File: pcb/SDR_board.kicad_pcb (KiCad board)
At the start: 4 copper layers, 100 x 100 mm, 469 parts, among them J1 USB_B_Mini, J201 Molex 73251-1150 SMA, J301 Molex 73251-1150 SMA, J401 Molex 73251-1150 SMA, J501 Molex 73251-1150 SMA, SW1 SW_Push, U1 AMS1117-3.3, U2 NB3L553, U201 BGA2803, U202 MSi001-Q40, U203 MAX19777AZA+, U204 ADS7883, U205 LMV712-N, U206 MAX19777AZA+, U207 ADS7883, U3 CY7C68013A-56PVX, U301 BGA2803, U302 MSi001-Q40, U303 MAX19777AZA+, U304 ADS7883, U305 LMV712-N, U306 MAX19777AZA+, U307 ADS7883, U401 BGA2803, U402 MSi001-Q40, U403 MAX19777AZA+, U404 ADS7883, U405 LMV712-N, U406 MAX19777AZA+, U407 ADS7883, U5 24LC128, U501 BGA2803, U502 MSi001-Q40, U503 MAX19777AZA+, U504 ADS7883, U505 LMV712-N, U506 MAX19777AZA+, U507 ADS7883, U6 MCP1825S, X1 XO32, X2 XO32

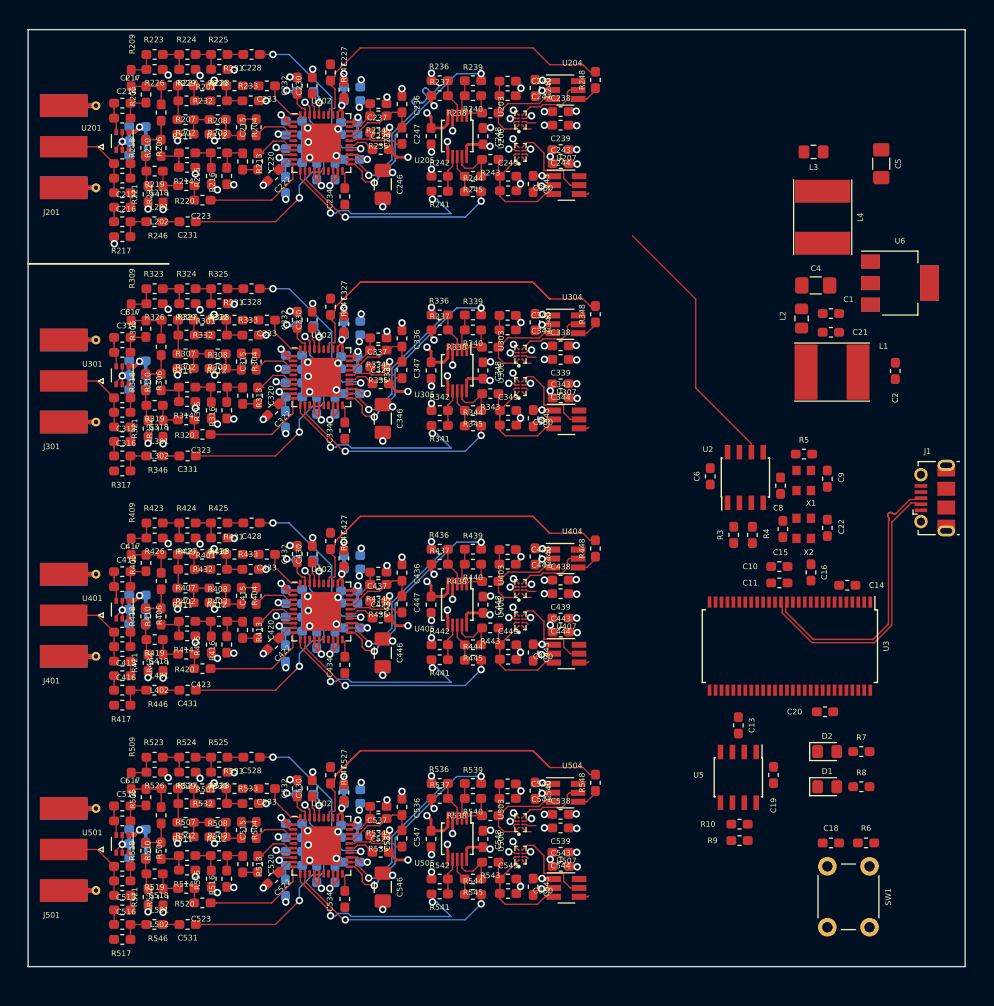
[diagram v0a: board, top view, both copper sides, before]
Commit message: silkscreen looks good for channel 1; TODO: copy to other channels.
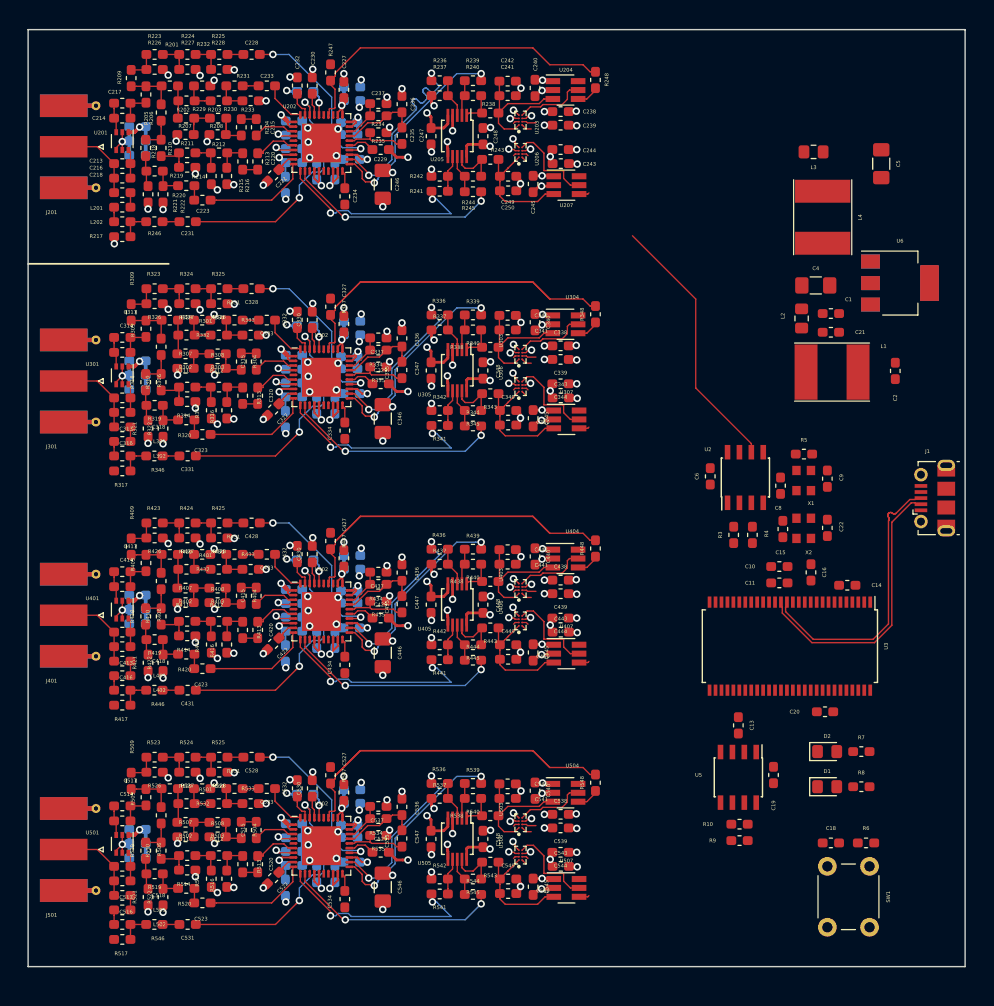
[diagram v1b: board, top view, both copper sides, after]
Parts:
- moved R202 0.16 mm to (41.9, 29.4)
- moved R203 0.16 mm to (45.3, 29.4)
- moved R207 0.05 mm to (41.8, 31.2)
- moved R208 0.05 mm to (45.2, 31.2)
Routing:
- net Net-(R203-Pad1): track 3.26 -> 5.03 mm
- net Net-(R202-Pad1): track 3.23 -> 4.02 mm
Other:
- rule pad_to_mask_clearance: 0.051 -> 0.03
- rule solder_mask_min_width: 0.25 -> 0.1

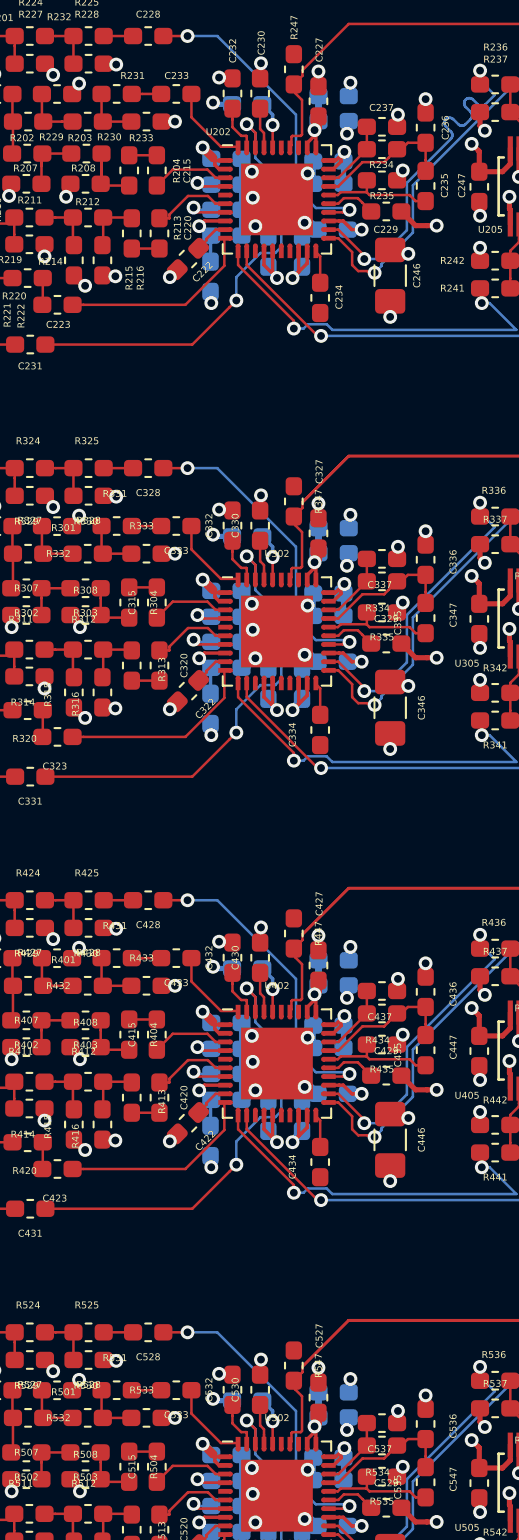
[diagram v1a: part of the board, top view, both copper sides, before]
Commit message: Closed solder resist around the MSi001 packages
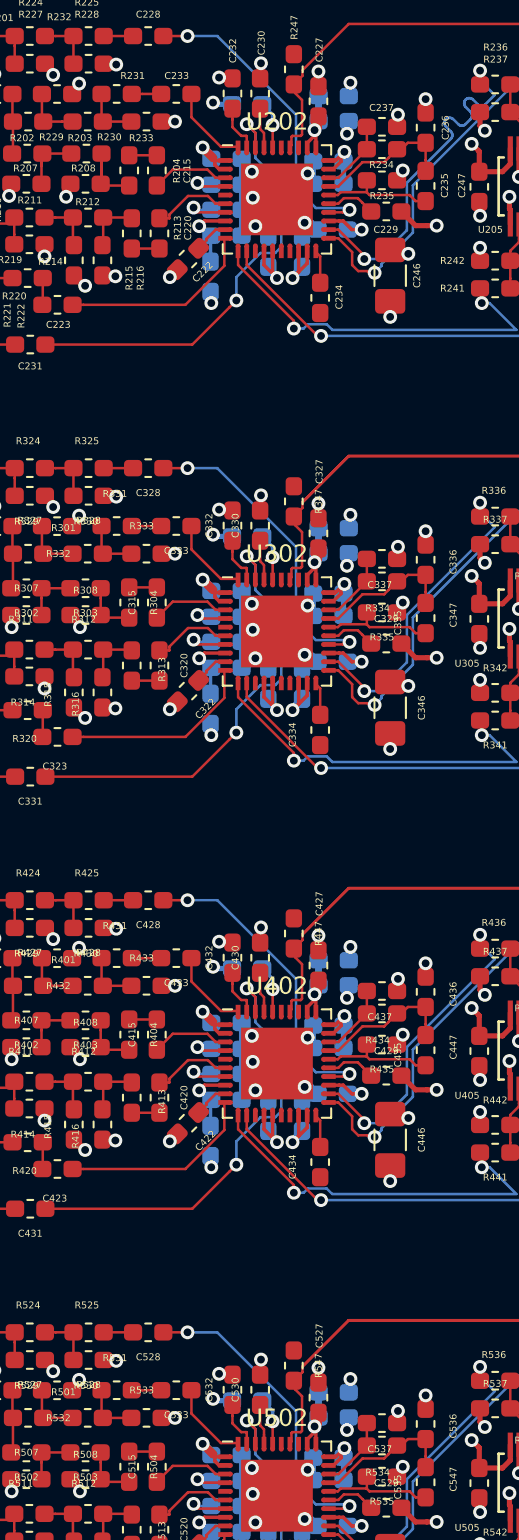
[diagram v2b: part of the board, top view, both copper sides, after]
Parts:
- U202, U302, U402, U502: footprint Package_DFN_QFN:Texas_S-PVQFN-N40_EP4.15x4.15mm -> footprints:Texas_S-PVQFN-N40_EP4.15x4.15mm_less_solder_resist

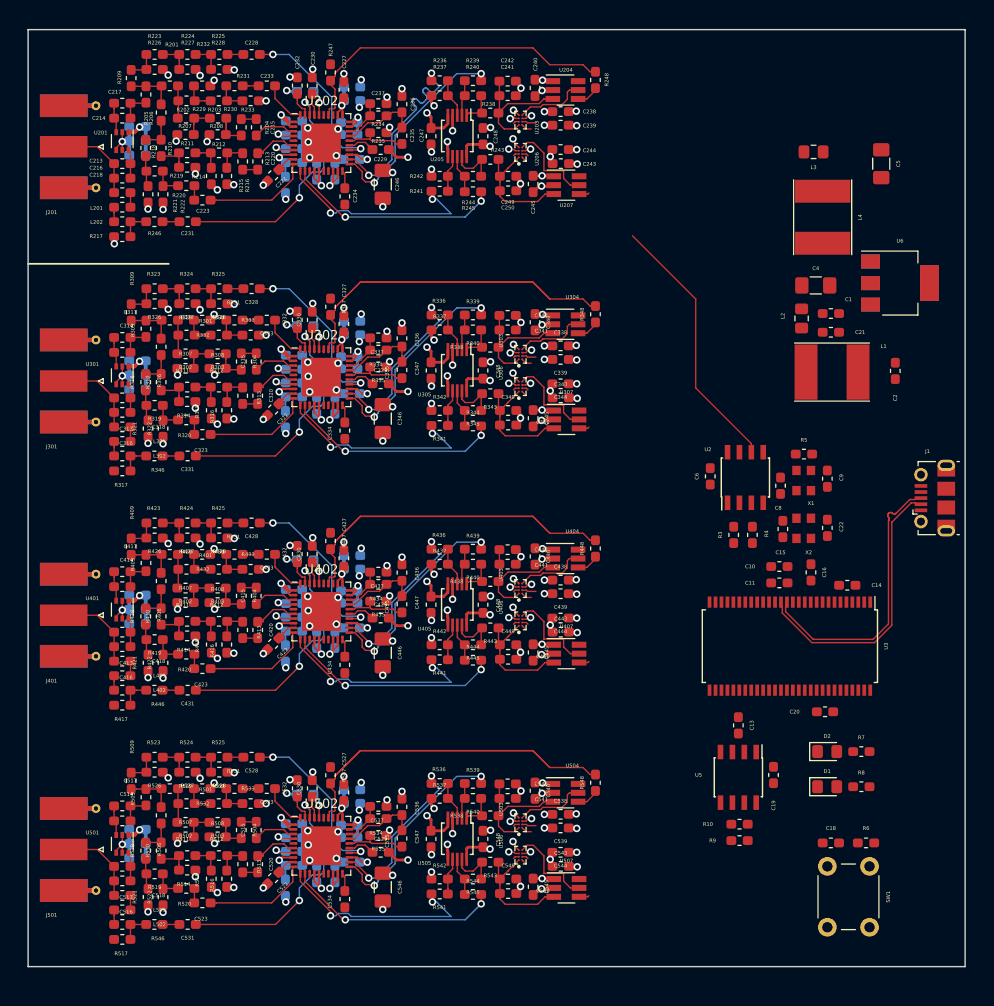
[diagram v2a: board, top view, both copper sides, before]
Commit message: Duplicated all those changes to chanel 1 through to the other channels
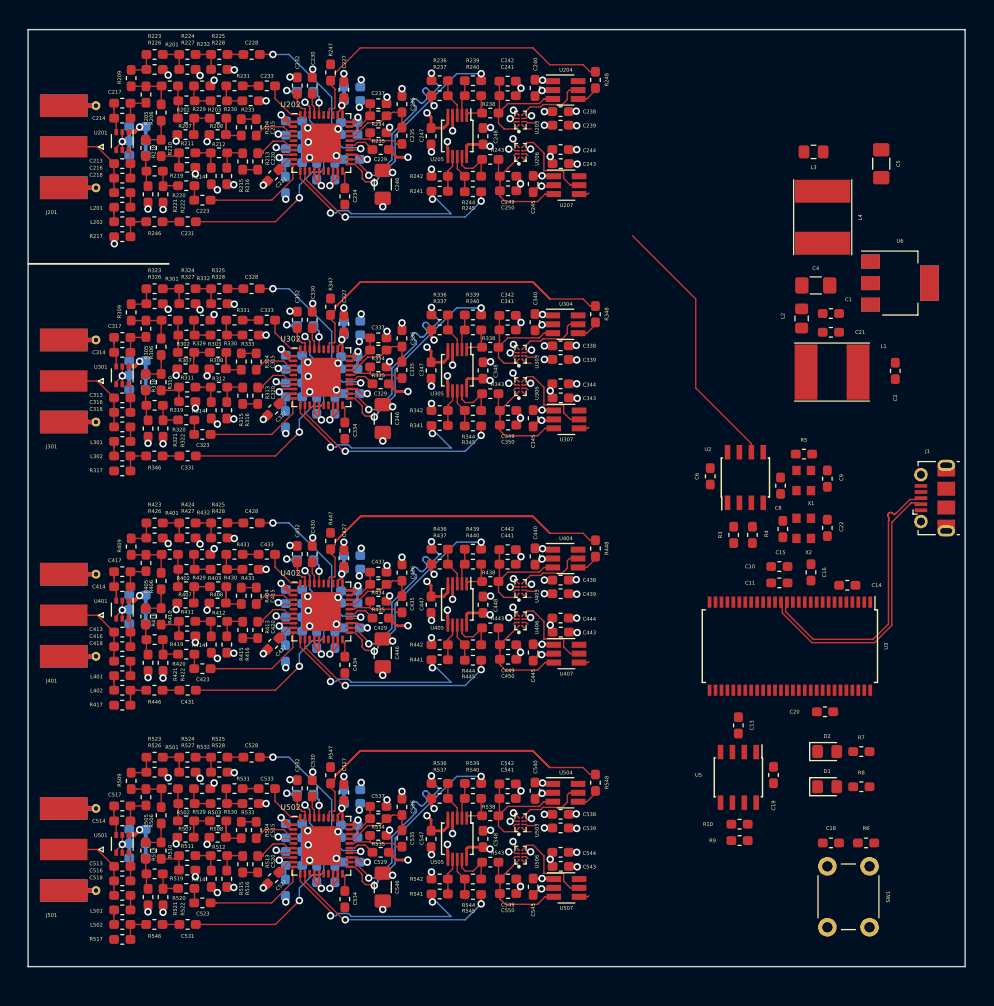
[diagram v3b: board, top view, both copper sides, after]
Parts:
- moved R302 0.16 mm to (41.9, 54.5)
- moved R303 0.16 mm to (45.3, 54.5)
- moved R402 0.16 mm to (41.9, 79.5)
- moved R502 0.16 mm to (41.9, 104.5)
- moved R403 0.16 mm to (45.3, 79.5)
- moved R503 0.16 mm to (45.3, 104.5)
- moved R307 0.05 mm to (41.8, 56.2)
- moved R308 0.05 mm to (45.2, 56.2)
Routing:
- net Net-(R347-Pad2): track 60.1 -> 109.6 mm
- net Net-(R547-Pad2): track 60.1 -> 109.6 mm
- net Net-(R447-Pad2): track 60.1 -> 109.6 mm
- net /Channel 2/Q_P: track 18.7 -> 21.7 mm
- net /Channel 4/Q_P: track 18.7 -> 21.7 mm
- net /Channel 3/Q_P: track 18.7 -> 21.7 mm
- net Net-(R303-Pad1): track 3.26 -> 5.03 mm
- net Net-(R503-Pad1): track 3.26 -> 5.03 mm
- net Net-(R403-Pad1): track 3.26 -> 5.03 mm
- net Net-(R302-Pad1): track 3.23 -> 4.02 mm
- net Net-(R502-Pad1): track 3.23 -> 4.02 mm
- net Net-(R402-Pad1): track 3.23 -> 4.02 mm
- net /Channel 4/Q_N: track 21.8 -> 22.6 mm
- net /Channel 3/Q_N: track 21.8 -> 22.6 mm
- net /Channel 2/Q_N: track 21.8 -> 22.6 mm

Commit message: simplified SPI clock source for the MSi001
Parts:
- removed R247, R248, R347, R348, R447, R448, R547, R548: 0R, Resistor_SMD:R_0603_1608Metric_Pad1.05x0.95mm_HandSolder
- added R1: 25, Resistor_SMD:R_0603_1608Metric_Pad1.05x0.95mm_HandSolder, F.Cu at (100.3, 61.6)
- added R2: 25, Resistor_SMD:R_0603_1608Metric_Pad1.05x0.95mm_HandSolder, F.Cu at (102.4, 61.6)
- moved C240 1.20 mm to (79.1, 25.0)
- moved U204 1.20 mm to (82.3, 25.2)
- moved C245 1.00 mm to (78.9, 37.5)
- moved U207 1.00 mm to (82.5, 37.6)
- moved C238 0.55 mm to (82.2, 28.4)
- moved C239 0.55 mm to (82.2, 29.8)
- moved C243 0.38 mm to (82.2, 34.4)
- moved C244 0.38 mm to (82.2, 32.9)
- moved C227 0.30 mm to (59.0, 26.4)
- moved R4 0.15 mm to (102.4, 73.9)
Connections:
- U2 pad 6: /TUNER_1_CLK -> Net-(R2-Pad1)
- U2 pad 7: /TUNER_2_CLK -> Net-(R1-Pad1)
- U202 pad 34: Net-(R247-Pad2) -> TUNER_SPI_CLK
- U302 pad 34: Net-(R347-Pad2) -> TUNER_SPI_CLK
- U402 pad 34: Net-(R447-Pad2) -> TUNER_SPI_CLK
- U502 pad 34: Net-(R547-Pad2) -> TUNER_SPI_CLK
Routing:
- net TUNER_SPI_CLK: track 0.00 -> 366.4 mm
- net Net-(R547-Pad2): track 109.6 -> 0.00 mm
- net Net-(R447-Pad2): track 109.6 -> 0.00 mm
- net Net-(R347-Pad2): track 109.6 -> 0.00 mm
- net TUNER_SPI_MOSI: track 0.00 -> 38.1 mm
- net /TUNER_1_nCS: track 0.00 -> 36.7 mm
- net Net-(R247-Pad2): track 35.3 -> 0.00 mm
- net /TUNER_1_CLK: track 28.4 -> 0.00 mm
- net ADC_nCS: track 8.90 -> 24.8 mm, vias 0 -> 2
- net ADC_CLK: track 23.7 -> 36.5 mm
- net /Channel 1/I_DOUT: track 9.73 -> 9.03 mm
- net +3.3VA: track 201.8 -> 201.6 mm, vias 76 -> 75

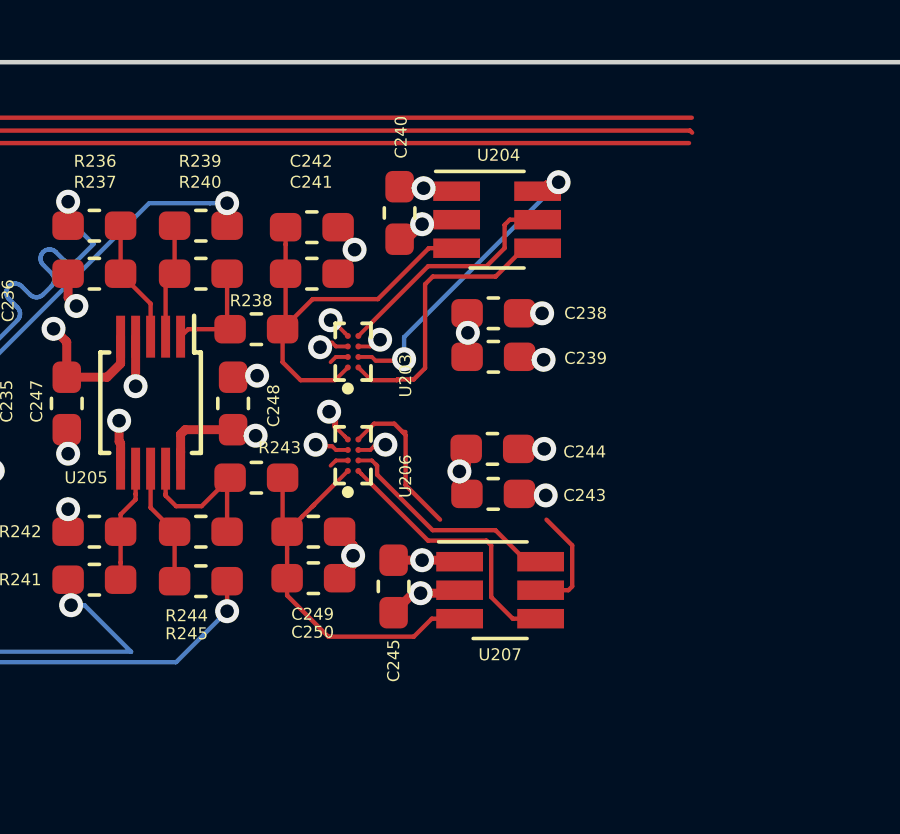
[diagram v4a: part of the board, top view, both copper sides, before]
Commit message: Finished signal routing for ADCs at the tuner side
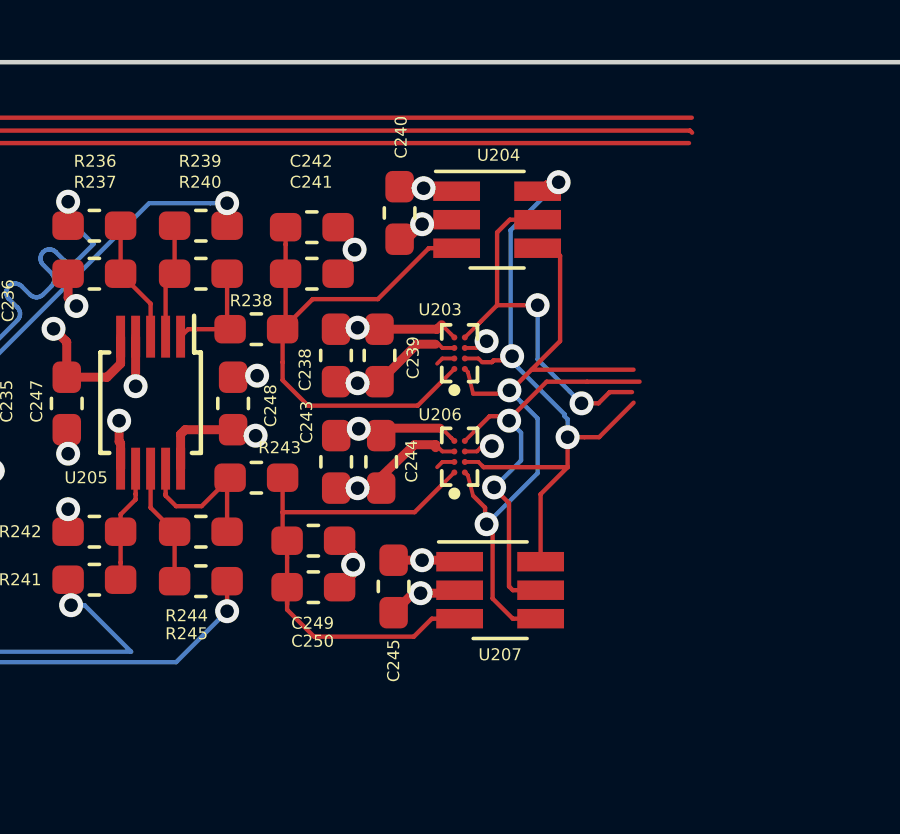
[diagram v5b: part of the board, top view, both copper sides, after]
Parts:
- moved C243 5.34 mm to (77.0, 33.3), turned to 270 degrees
- moved C239 5.25 mm to (77.0, 29.8), turned to 90 degrees
- moved C238 4.05 mm to (78.4, 29.8), turned to 270 degrees
- moved C244 3.73 mm to (78.5, 33.3), turned to 90 degrees
- moved U203 3.55 mm to (81.1, 29.7)
- moved U206 3.55 mm to (81.1, 33.1)
- moved C249 0.30 mm to (76.2, 36.0)
- moved C250 0.30 mm to (76.2, 37.5)
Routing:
- net ADC_nCS: track 24.8 -> 30.6 mm, vias 2 -> 3
- net ADC_CLK: track 36.5 -> 42.0 mm, vias 0 -> 2
- net /Channel 1/I_DOUT: track 9.03 -> 14.3 mm, vias 0 -> 2
- net /Channel 1/Q_DOUT: track 8.03 -> 12.7 mm, vias 0 -> 2
- net /Channel 1/BUFFERED_SINGLE_Q: track 14.1 -> 18.6 mm
- net /Channel 1/BUFFERED_SINGLE_I: track 13.5 -> 17.7 mm
- net GND: track 317.8 -> 322.0 mm, vias 193 -> 189
- net +3.3VA: track 201.6 -> 205.2 mm, vias 75 -> 73
